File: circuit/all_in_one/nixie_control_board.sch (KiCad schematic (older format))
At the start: 1 part

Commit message: [All in one]Construct mode circuits
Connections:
- wire segments 15 -> 22
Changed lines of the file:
@@
 F3 "5V" I L 5300 3700 60
 F4 "GND" I L 5300 3900 60
+F5 "I2C_SCL" I R 6250 3500 60
+F6 "I2C_SDA" I R 6250 3700 60
 $EndSheet
 $Comp
@@
 	3600 3750 3800 3750
 Wire Wire Line
-	3800 3750 3800 4250
+	3800 3750 3800 4350
 Wire Wire Line
 	3800 3800 3950 3800
-Wire Wire Line
-	3800 4250 5100 4250
-Wire Wire Line
-	5100 4250 5100 3900
-Wire Wire Line
-	5100 3900 5300 3900
 Connection ~ 3800 3800
-Wire Wire Line
-	4900 3800 5100 3800
-Wire Wire Line
-	5100 3800 5100 3700
-Wire Wire Line
-	5100 3700 5300 3700
-Wire Wire Line
-	4950 3600 5100 3600
-Wire Wire Line
-	5100 3600 5100 3500
-Wire Wire Line
-	5100 3500 5300 3500
 $Sheet
-S 5300 2200 950  800
+S 6700 3300 950  1000
 U 5646A754
 F0 "RTC" 98
 F1 "RTC.sch" 98
+F2 "I2C_SCL" I L 6700 3500 60
+F3 "I2C_SDA" I L 6700 3700 60
+F4 "5V" I L 6700 3900 60
+F5 "GND" I L 6700 4100 60
 $EndSheet
 $Sheet
-S 5300 4450 950  800
+S 6700 2100 950  800
 U 5646A864
 F0 "audio" 98
@@
 $EndSheet
 $Sheet
-S 6700 3300 950  800
+S 5300 2100 950  800
 U 5646AE2C
 F0 "display" 98
 F1 "display.sch" 98
 $EndSheet
+Wire Wire Line
+	6700 3500 6250 3500
+Wire Wire Line
+	6250 3700 6700 3700
+Wire Wire Line
+	5100 4250 6450 4250
+Wire Wire Line
+	6450 4250 6450 3900
+Wire Wire Line
+	6450 3900 6700 3900
+Wire Wire Line
+	3800 4350 6550 4350
+Wire Wire Line
+	6550 4350 6550 4100
+Wire Wire Line
+	6550 4100 6700 4100
+Wire Wire Line
+	4900 3600 5100 3600
+Wire Wire Line
+	5100 3600 5100 3500
+Wire Wire Line
+	5100 3500 5300 3500
+Wire Wire Line
+	4900 3800 5100 3800
+Wire Wire Line
+	5100 3700 5100 4250
+Wire Wire Line
+	5100 3700 5300 3700
+Connection ~ 5100 3800
+Wire Wire Line
+	5300 3900 5200 3900
+Wire Wire Line
+	5200 3900 5200 4350
+Connection ~ 5200 4350
 $EndSCHEMATC

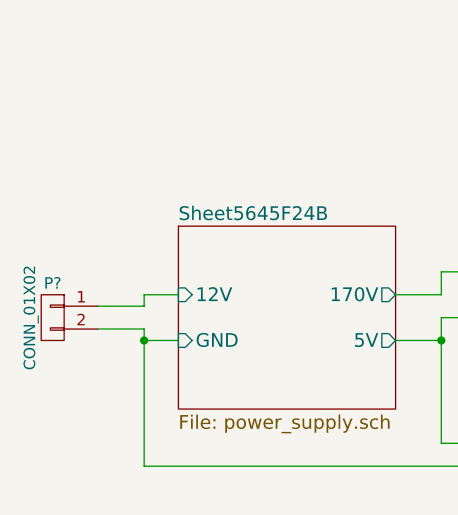
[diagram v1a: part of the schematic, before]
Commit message: [All in one]Define part of compoment's footprint
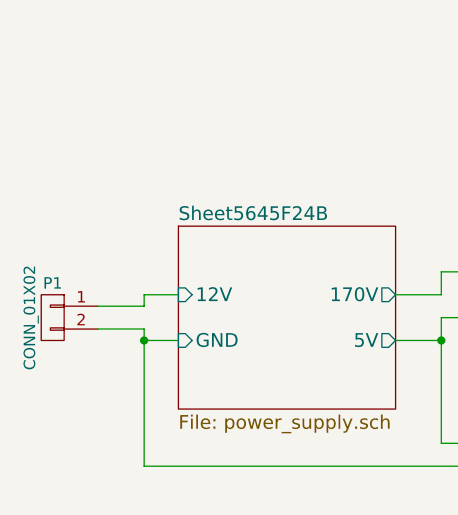
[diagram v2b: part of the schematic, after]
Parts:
- gave numbers to parts that had none: 1
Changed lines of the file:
@@
 $EndSheet
 $Comp
-L CONN_01X02 P?
+L CONN_01X02 P1
 U 1 1 56461034
 P 3400 3700
-F 0 "P?" H 3400 3850 50  0000 C CNN
+F 0 "P1" H 3400 3850 50  0000 C CNN
 F 1 "CONN_01X02" V 3500 3700 50  0000 C CNN
-F 2 "" H 3400 3700 60  0000 C CNN
+F 2 "" H 3400 3700 60  0001 C CNN
 F 3 "" H 3400 3700 60  0000 C CNN
 	1    3400 3700

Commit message: [IN-14]Add IN-14 circuit
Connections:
- net Sheet5645F24B/12V renamed power_supply/12V
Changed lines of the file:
@@
 S 3950 3300 950  800
 U 5645F24C
-F0 "Sheet5645F24B" 60
+F0 "power_supply" 60
 F1 "power_supply.sch" 60
 F2 "170V" O R 4900 3600 60

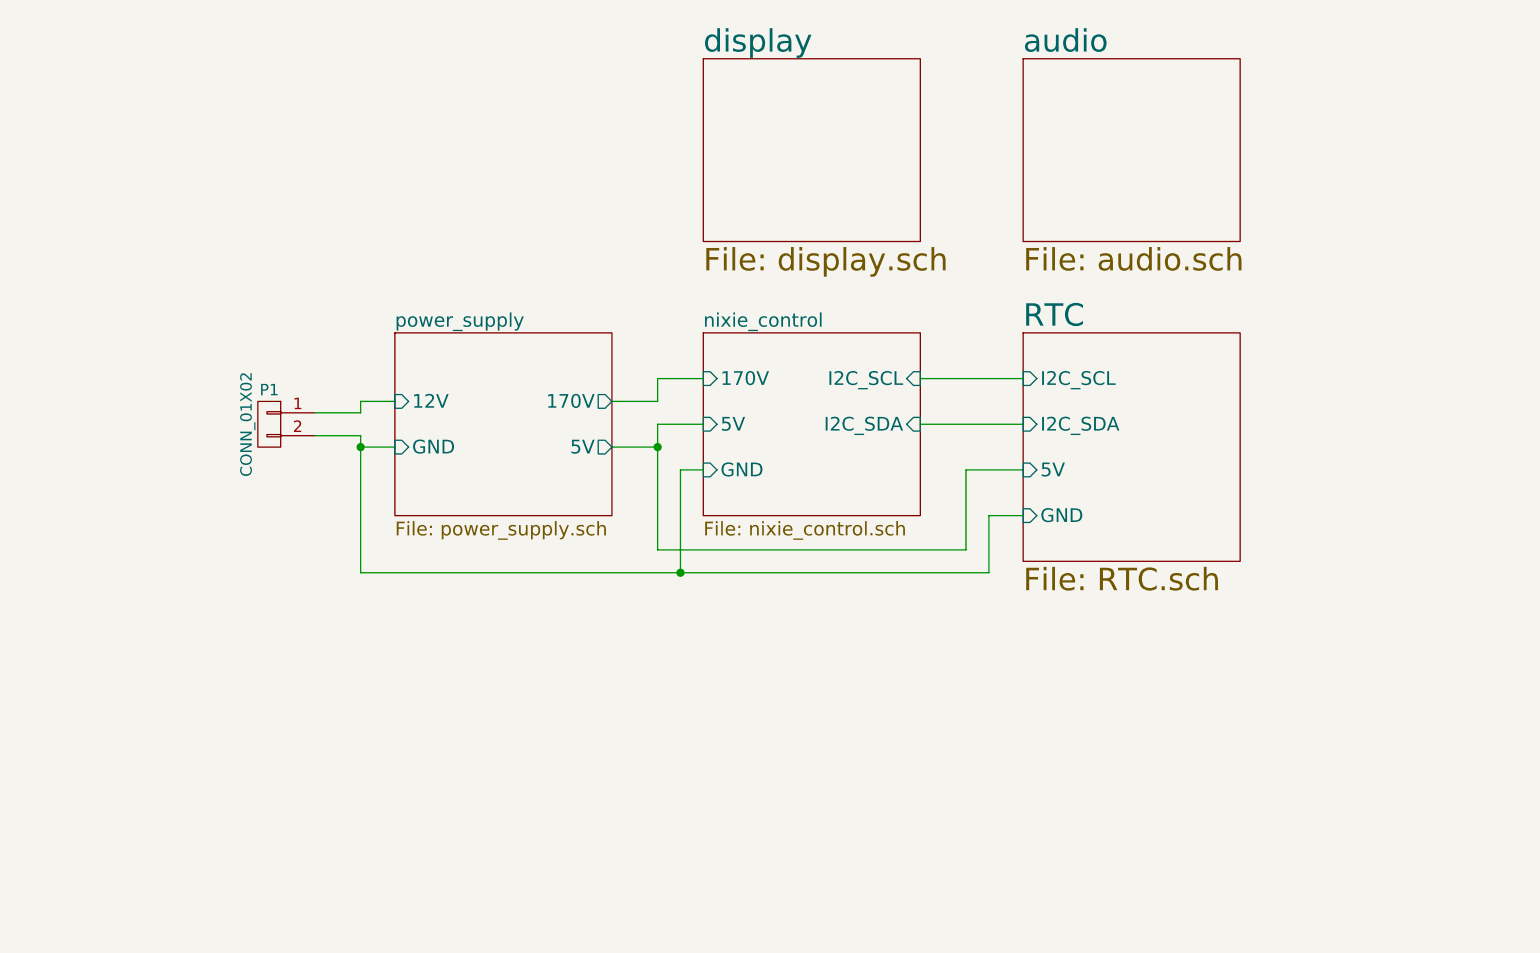
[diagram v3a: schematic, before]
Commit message: [All in one]Finish the tube display circuit
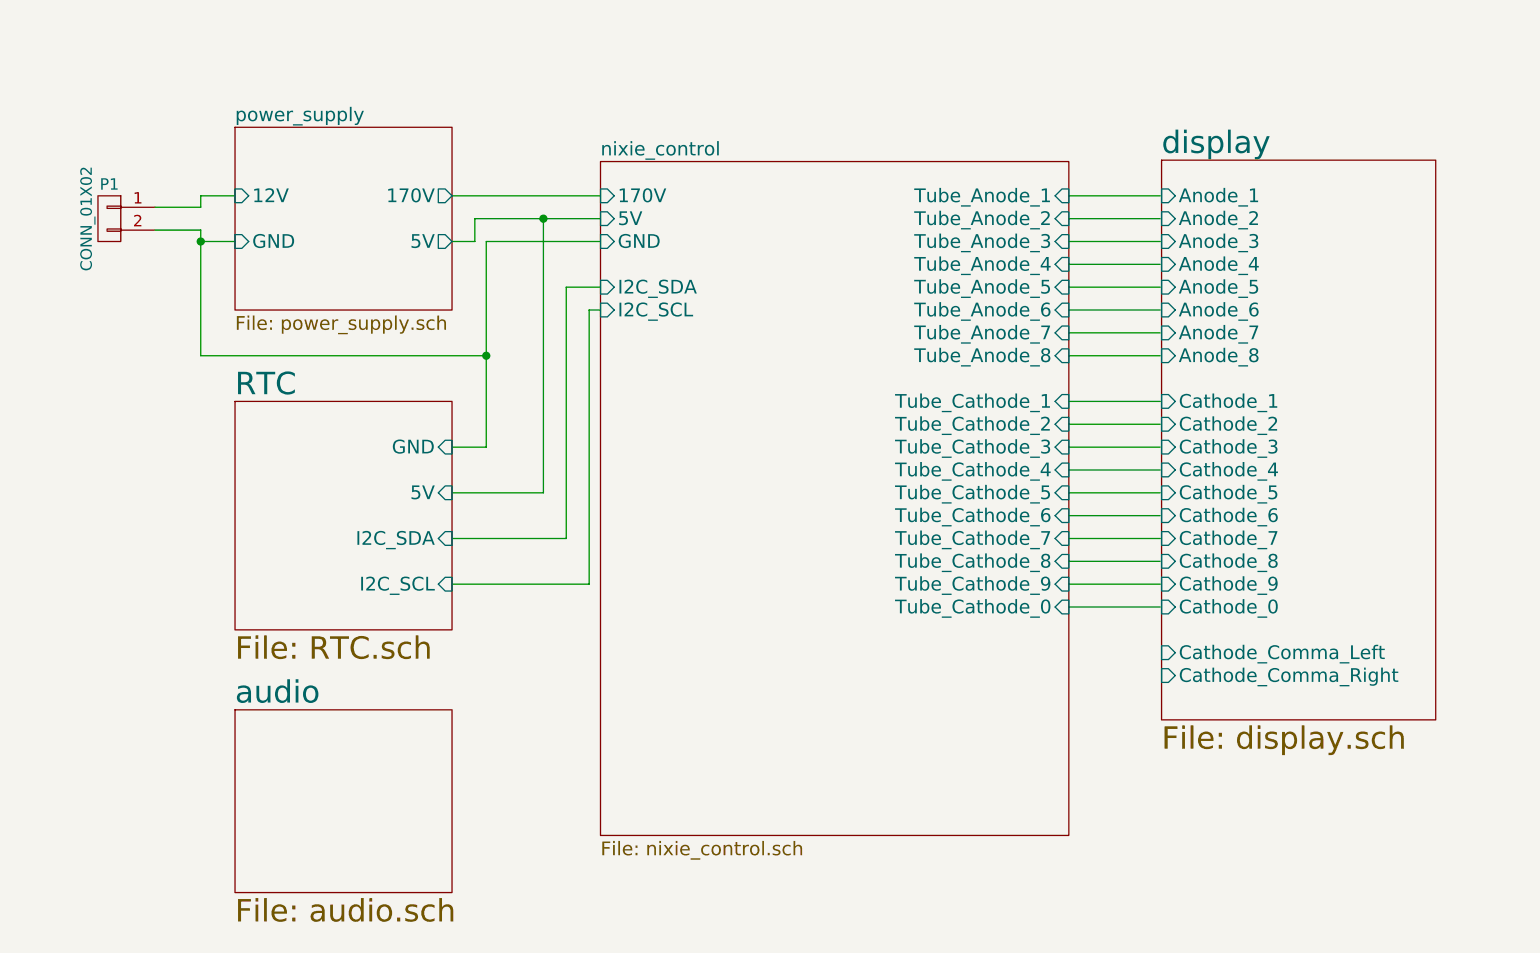
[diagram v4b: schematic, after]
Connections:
- wire segments 22 -> 40
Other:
- moved on the sheet: P1
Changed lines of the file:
@@
 $EndDescr
 $Sheet
-S 3950 3300 950  800
+S 3250 2400 950  800
 U 5645F24C
 F0 "power_supply" 60
 F1 "power_supply.sch" 60
-F2 "170V" O R 4900 3600 60
-F3 "5V" O R 4900 3800 60
-F4 "12V" I L 3950 3600 60
-F5 "GND" I L 3950 3800 60
+F2 "170V" O R 4200 2700 60
+F3 "5V" O R 4200 2900 60
+F4 "12V" I L 3250 2700 60
+F5 "GND" I L 3250 2900 60
 $EndSheet
 $Sheet
-S 5300 3300 950  800
+S 4850 2550 2050 2950
 U 5645F2A4
 F0 "nixie_control" 60
 F1 "nixie_control.sch" 60
-F2 "170V" I L 5300 3500 60
-F3 "5V" I L 5300 3700 60
-F4 "GND" I L 5300 3900 60
-F5 "I2C_SCL" I R 6250 3500 60
-F6 "I2C_SDA" I R 6250 3700 60
+F2 "170V" I L 4850 2700 60
+F3 "5V" I L 4850 2800 60
+F4 "GND" I L 4850 2900 60
+F5 "I2C_SCL" I L 4850 3200 60
+F6 "I2C_SDA" I L 4850 3100 60
+F7 "Tube_Anode_1" I R 6900 2700 60
+F8 "Tube_Anode_2" I R 6900 2800 60
+F9 "Tube_Anode_3" I R 6900 2900 60
+F10 "Tube_Anode_4" I R 6900 3000 60
+F11 "Tube_Anode_5" I R 6900 3100 60
+F12 "Tube_Anode_6" I R 6900 3200 60
+F13 "Tube_Anode_7" I R 6900 3300 60
+F14 "Tube_Anode_8" I R 6900 3400 60
+F15 "Tube_Cathode_0" I R 6900 4500 60
+F16 "Tube_Cathode_1" I R 6900 3600 60
+F17 "Tube_Cathode_2" I R 6900 3700 60
+F18 "Tube_Cathode_3" I R 6900 3800 60
+F19 "Tube_Cathode_4" I R 6900 3900 60
+F20 "Tube_Cathode_5" I R 6900 4000 60
+F21 "Tube_Cathode_6" I R 6900 4100 60
+F22 "Tube_Cathode_7" I R 6900 4200 60
+F23 "Tube_Cathode_8" I R 6900 4300 60
+F24 "Tube_Cathode_9" I R 6900 4400 60
 $EndSheet
 $Comp
 L CONN_01X02 P1
 U 1 1 56461034
-P 3400 3700
-F 0 "P1" H 3400 3850 50  0000 C CNN
-F 1 "CONN_01X02" V 3500 3700 50  0000 C CNN
-F 2 "" H 3400 3700 60  0001 C CNN
-F 3 "" H 3400 3700 60  0000 C CNN
-	1    3400 3700
+P 2700 2800
+F 0 "P1" H 2700 2950 50  0000 C CNN
+F 1 "CONN_01X02" V 2800 2800 50  0000 C CNN
+F 2 "" H 2700 2800 60  0001 C CNN
+F 3 "" H 2700 2800 60  0000 C CNN
+	1    2700 2800
 	-1   0    0    -1
 $EndComp
-Wire Wire Line
-	3600 3650 3800 3650
-Wire Wire Line
-	3800 3650 3800 3600
-Wire Wire Line
-	3800 3600 3950 3600
-Wire Wire Line
-	3600 3750 3800 3750
-Wire Wire Line
-	3800 3750 3800 4350
-Wire Wire Line
-	3800 3800 3950 3800
-Connection ~ 3800 3800
 $Sheet
-S 6700 3300 950  1000
+S 3250 3600 950  1000
 U 5646A754
 F0 "RTC" 98
 F1 "RTC.sch" 98
-F2 "I2C_SCL" I L 6700 3500 60
-F3 "I2C_SDA" I L 6700 3700 60
-F4 "5V" I L 6700 3900 60
-F5 "GND" I L 6700 4100 60
+F2 "I2C_SCL" I R 4200 4400 60
+F3 "I2C_SDA" I R 4200 4200 60
+F4 "5V" I R 4200 4000 60
+F5 "GND" I R 4200 3800 60
 $EndSheet
 $Sheet
-S 6700 2100 950  800
+S 3250 4950 950  800
 U 5646A864
 F0 "audio" 98
@@
 $EndSheet
 $Sheet
-S 5300 2100 950  800
+S 7306 2544 1200 2450
 U 5646AE2C
 F0 "display" 98
 F1 "display.sch" 98
+F2 "Anode_2" I L 7306 2800 60
+F3 "Anode_1" I L 7306 2700 60
+F4 "Anode_3" I L 7306 2900 60
+F5 "Anode_4" I L 7306 3000 60
+F6 "Anode_5" I L 7306 3100 60
+F7 "Anode_6" I L 7306 3200 60
+F8 "Anode_7" I L 7306 3300 60
+F9 "Anode_8" I L 7306 3400 60
+F10 "Cathode_4" I L 7306 3900 60
+F11 "Cathode_3" I L 7306 3800 60
+F12 "Cathode_2" I L 7306 3700 60
+F13 "Cathode_1" I L 7306 3600 60
+F14 "Cathode_Comma_Right" I L 7306 4800 60
+F15 "Cathode_Comma_Left" I L 7306 4700 60
+F16 "Cathode_5" I L 7306 4000 60
+F17 "Cathode_6" I L 7306 4100 60
+F18 "Cathode_7" I L 7306 4200 60
+F19 "Cathode_8" I L 7306 4300 60
+F20 "Cathode_9" I L 7306 4400 60
+F21 "Cathode_0" I L 7306 4500 60
 $EndSheet
 Wire Wire Line
-	6700 3500 6250 3500
+	2900 2750 3100 2750
 Wire Wire Line
-	6250 3700 6700 3700
+	3100 2750 3100 2700
 Wire Wire Line
-	5100 4250 6450 4250
+	3100 2700 3250 2700
 Wire Wire Line
-	6450 4250 6450 3900
+	2900 2850 3100 2850
 Wire Wire Line
-	6450 3900 6700 3900
+	3100 2900 3250 2900
 Wire Wire Line
-	3800 4350 6550 4350
+	3100 2850 3100 3400
 Wire Wire Line
-	6550 4350 6550 4100
+	7300 2700 6900 2700
 Wire Wire Line
-	6550 4100 6700 4100
+	7300 2800 6900 2800
 Wire Wire Line
-	4900 3600 5100 3600
+	7300 2900 6900 2900
 Wire Wire Line
-	5100 3600 5100 3500
+	7300 3000 6900 3000
 Wire Wire Line
-	5100 3500 5300 3500
+	7300 3100 6900 3100
 Wire Wire Line
-	4900 3800 5100 3800
+	7300 3200 6900 3200
 Wire Wire Line
-	5100 3700 5100 4250
+	7300 3300 6900 3300
 Wire Wire Line
-	5100 3700 5300 3700
-Connection ~ 5100 3800
+	7300 3400 6900 3400
 Wire Wire Line
-	5300 3900 5200 3900
+	7300 3600 6900 3600
 Wire Wire Line
-	5200 3900 5200 4350
-Connection ~ 5200 4350
+	7300 3700 6900 3700
+Wire Wire Line
+	7300 3800 6900 3800
+Wire Wire Line
+	6900 3900 7300 3900
+Wire Wire Line
+	7300 4000 6900 4000
+Wire Wire Line
+	7300 4100 6900 4100
+Wire Wire Line
+	7300 4200 6900 4200
+Wire Wire Line
+	7300 4300 6900 4300
+Wire Wire Line
+	7300 4400 6900 4400
+Wire Wire Line
+	7300 4500 6900 4500
+Wire Wire Line
+	4200 2700 4850 2700
+Wire Wire Line
+	4200 2900 4300 2900
+Wire Wire Line
+	4300 2900 4300 2800
+Wire Wire Line
+	4300 2800 4850 2800
+Wire Wire Line
+	3100 3400 4350 3400
+Wire Wire Line
+	4350 2900 4350 3800
+Wire Wire Line
+	4350 2900 4850 2900
+Connection ~ 3100 2900
+Wire Wire Line
+	4600 2800 4600 4000
+Wire Wire Line
+	4600 4000 4200 4000
+Connection ~ 4600 2800
+Wire Wire Line
+	4350 3800 4200 3800
+Connection ~ 4350 3400
+Wire Wire Line
+	4200 4200 4700 4200
+Wire Wire Line
+	4700 4200 4700 3100
+Wire Wire Line
+	4700 3100 4850 3100
+Wire Wire Line
+	4850 3200 4800 3200
+Wire Wire Line
+	4800 3200 4800 4400
+Wire Wire Line
+	4800 4400 4200 4400
 $EndSCHEMATC

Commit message: [All in one]Add tube comma control circuit
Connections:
- wire segments 40 -> 42
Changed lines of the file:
@@
 F23 "Tube_Cathode_8" I R 6900 4300 60
 F24 "Tube_Cathode_9" I R 6900 4400 60
+F25 "Tube_Cathode_Comma_Left" I R 6900 4700 60
+F26 "Tube_Cathode_Comma_Right" I R 6900 4800 60
 $EndSheet
 $Comp
@@
 Wire Wire Line
 	4800 4400 4200 4400
+Wire Wire Line
+	7300 4700 6900 4700
+Wire Wire Line
+	7300 4800 6900 4800
 $EndSCHEMATC

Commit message: [All in one]Select resister and power jack's footprint
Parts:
- removed P1: CONN_01X02, symbol CONN_01X02
- added CON1: BARREL_JACK, Connect:JACK_ALIM, symbol BARREL_JACK
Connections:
- wire segments 42 -> 46
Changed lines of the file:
@@
 F25 "Tube_Cathode_Comma_Left" I R 6900 4700 60
 F26 "Tube_Cathode_Comma_Right" I R 6900 4800 60
+F27 "MP3_TX" I L 4850 5100 60
+F28 "MP3_RX" I L 4850 5200 60
 $EndSheet
-$Comp
-L CONN_01X02 P1
-U 1 1 56461034
-P 2700 2800
-F 0 "P1" H 2700 2950 50  0000 C CNN
-F 1 "CONN_01X02" V 2800 2800 50  0000 C CNN
-F 2 "" H 2700 2800 60  0001 C CNN
-F 3 "" H 2700 2800 60  0000 C CNN
-	1    2700 2800
-	-1   0    0    -1
-$EndComp
 $Sheet
 S 3250 3600 950  1000
@@
 F0 "audio" 98
 F1 "audio.sch" 98
+F2 "MCU_MP3_TX" I R 4200 5200 60
+F3 "MCU_MP3_RX" I R 4200 5300 60
 $EndSheet
 $Sheet
@@
 F21 "Cathode_0" I L 7306 4500 60
 $EndSheet
+$Comp
+L BARREL_JACK CON1
+U 1 1 5657C68E
+P 2650 2800
+F 0 "CON1" H 2650 3050 60  0000 C CNN
+F 1 "BARREL_JACK" H 2650 2600 60  0000 C CNN
+F 2 "Connect:JACK_ALIM" H 2650 2800 60  0001 C CNN
+F 3 "" H 2650 2800 60  0000 C CNN
+	1    2650 2800
+	1    0    0    -1
+$EndComp
 Wire Wire Line
-	2900 2750 3100 2750
+	2950 2700 3250 2700
 Wire Wire Line
-	3100 2750 3100 2700
+	2950 2900 3250 2900
 Wire Wire Line
-	3100 2700 3250 2700
-Wire Wire Line
-	2900 2850 3100 2850
-Wire Wire Line
-	3100 2900 3250 2900
-Wire Wire Line
-	3100 2850 3100 3400
+	3100 2900 3100 3400
 Wire Wire Line
 	7300 2700 6900 2700
@@
 Wire Wire Line
 	7300 4800 6900 4800
+Wire Wire Line
+	4200 5200 4500 5200
+Wire Wire Line
+	4500 5200 4500 5100
+Wire Wire Line
+	4500 5100 4850 5100
+Wire Wire Line
+	4200 5300 4600 5300
+Wire Wire Line
+	4600 5300 4600 5200
+Wire Wire Line
+	4600 5200 4850 5200
+Wire Wire Line
+	2950 2800 2950 2900
 $EndSCHEMATC
